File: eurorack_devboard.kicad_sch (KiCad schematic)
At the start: 13 parts, among them U1 STM32G474VETx

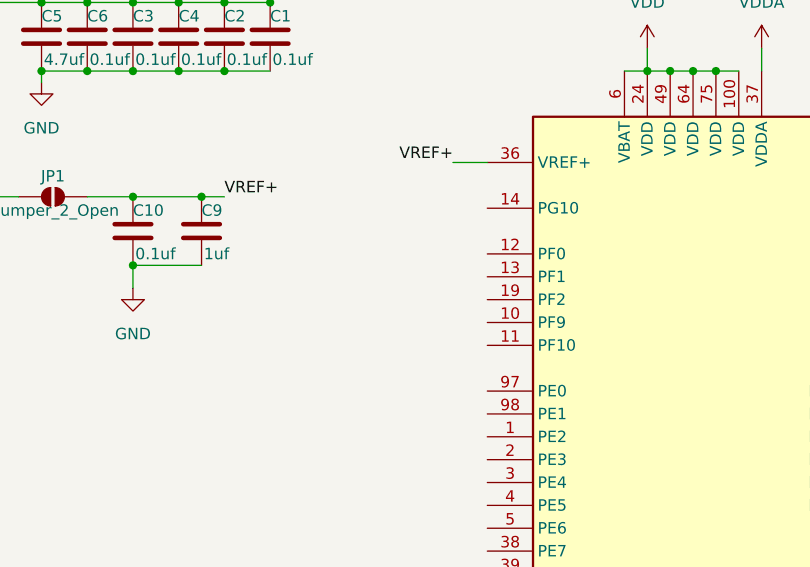
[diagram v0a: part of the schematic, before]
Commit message: Added reset capacitor and button
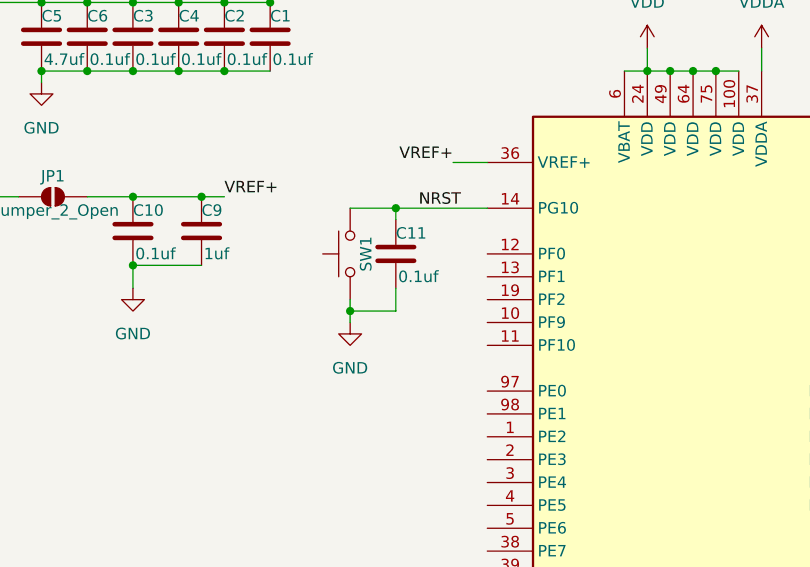
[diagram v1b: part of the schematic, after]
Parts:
- added C11: 0.1uf, symbol Device:C
- added SW1: SW_Push, symbol Switch:SW_Push
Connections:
- net GND: now also C11.2, SW1.1
- net NRST: now reaches U1.14 (PG10)
- net NRST: now also C11.1, SW1.2
